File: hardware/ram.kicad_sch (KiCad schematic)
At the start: 1 part, among them U901 MT53E512M32D1ZW-046 WT:B

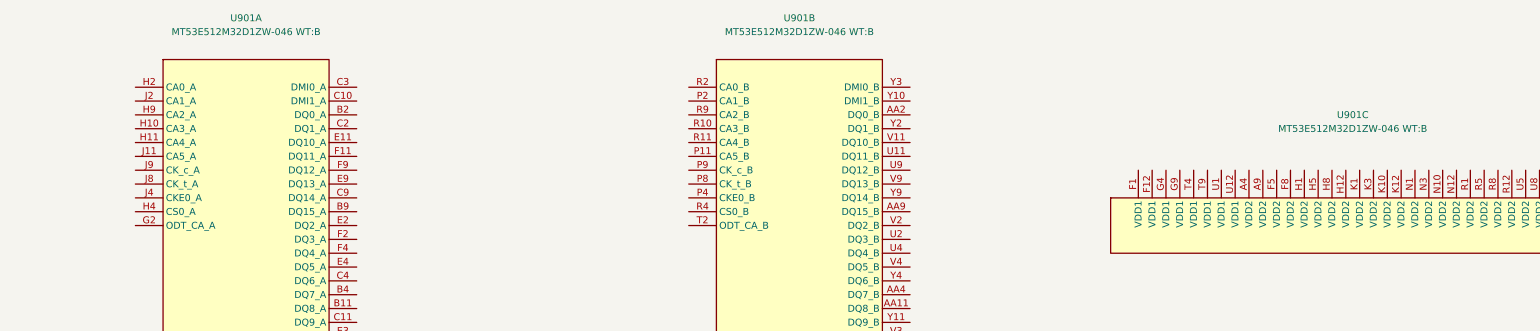
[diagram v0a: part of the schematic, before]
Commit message: Connect RAM VDD1 and LPDDR4X ODT controls
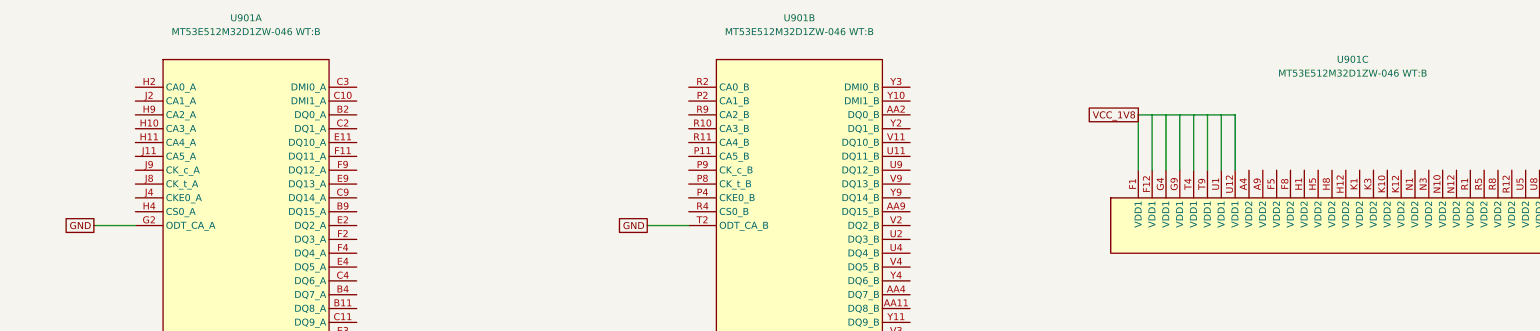
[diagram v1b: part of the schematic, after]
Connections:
- net GND: now also U901.G2 (ODT_CA_A), U901.T2 (ODT_CA_B)
- net VCC_1V8: now reaches U901.F1 (VDD1)
- net VCC_1V8: now also U901.U12 (VDD1)

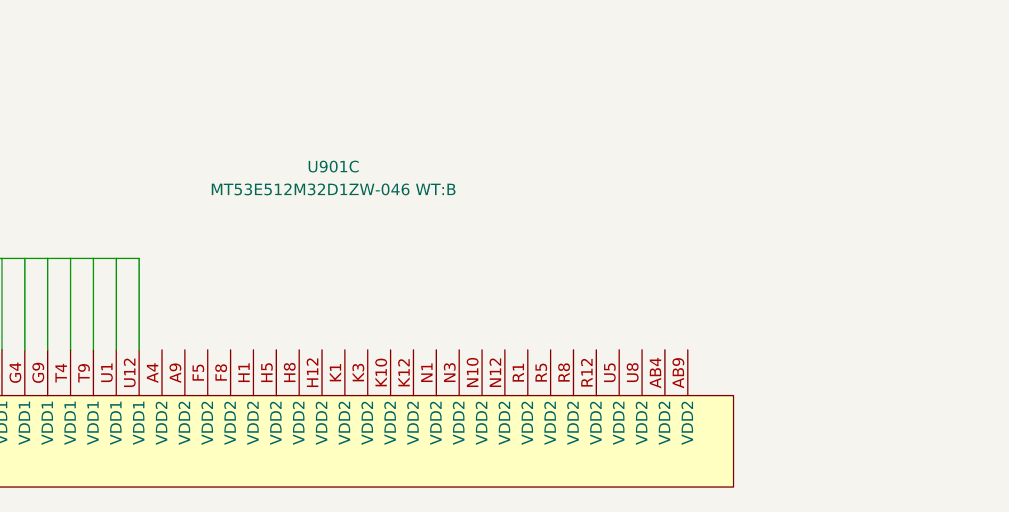
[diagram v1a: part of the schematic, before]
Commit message: Capture DDR BUCK3 supply and RAM VDD2 connections
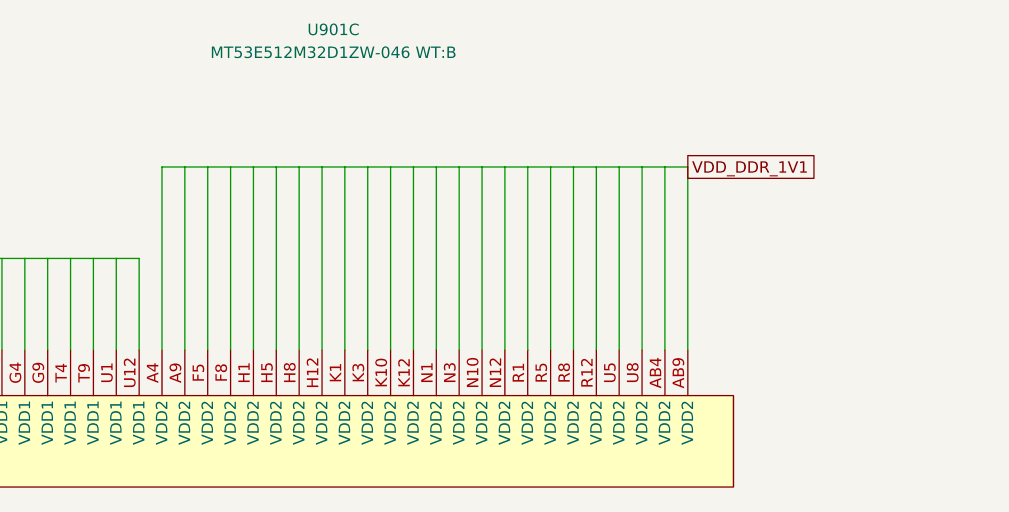
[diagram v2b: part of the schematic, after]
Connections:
- net VDD_DDR_1V1: now reaches U901.A4 (VDD2)
- net VDD_DDR_1V1: now also U901.AB9 (VDD2)

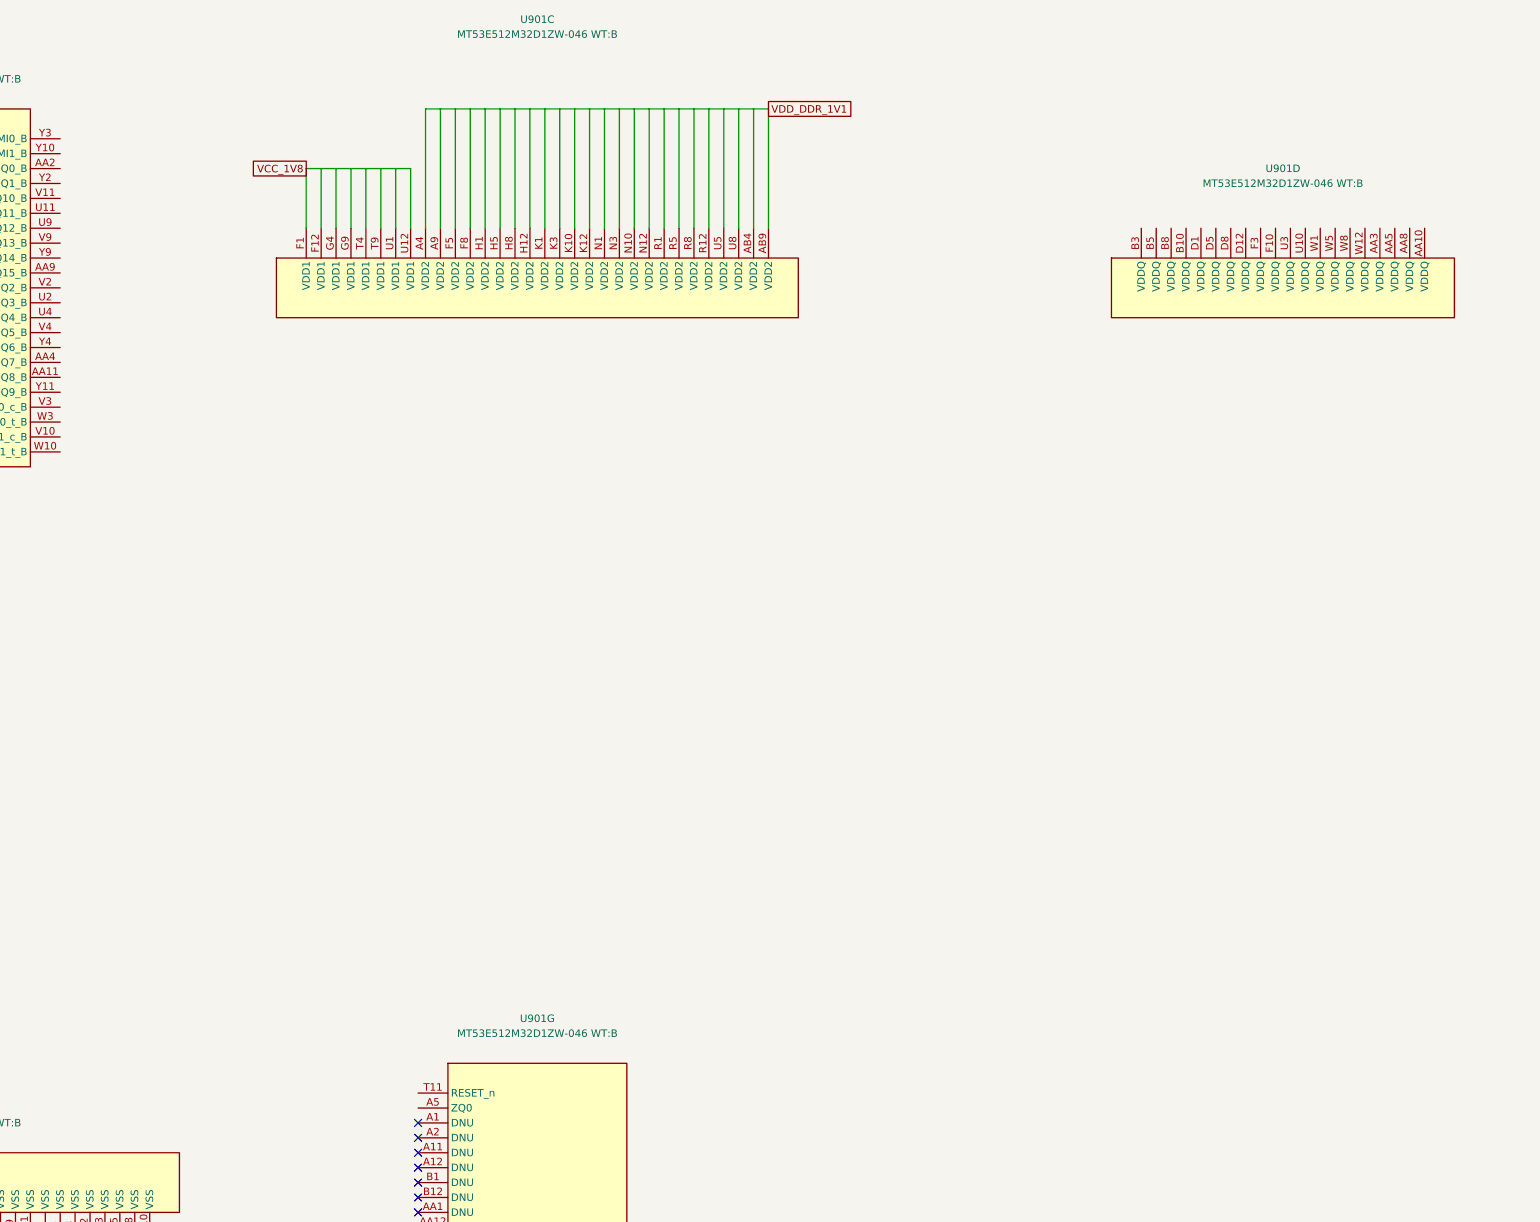
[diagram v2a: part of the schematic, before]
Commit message: Capture RAM ZQ calibration and separate VDDQ domain
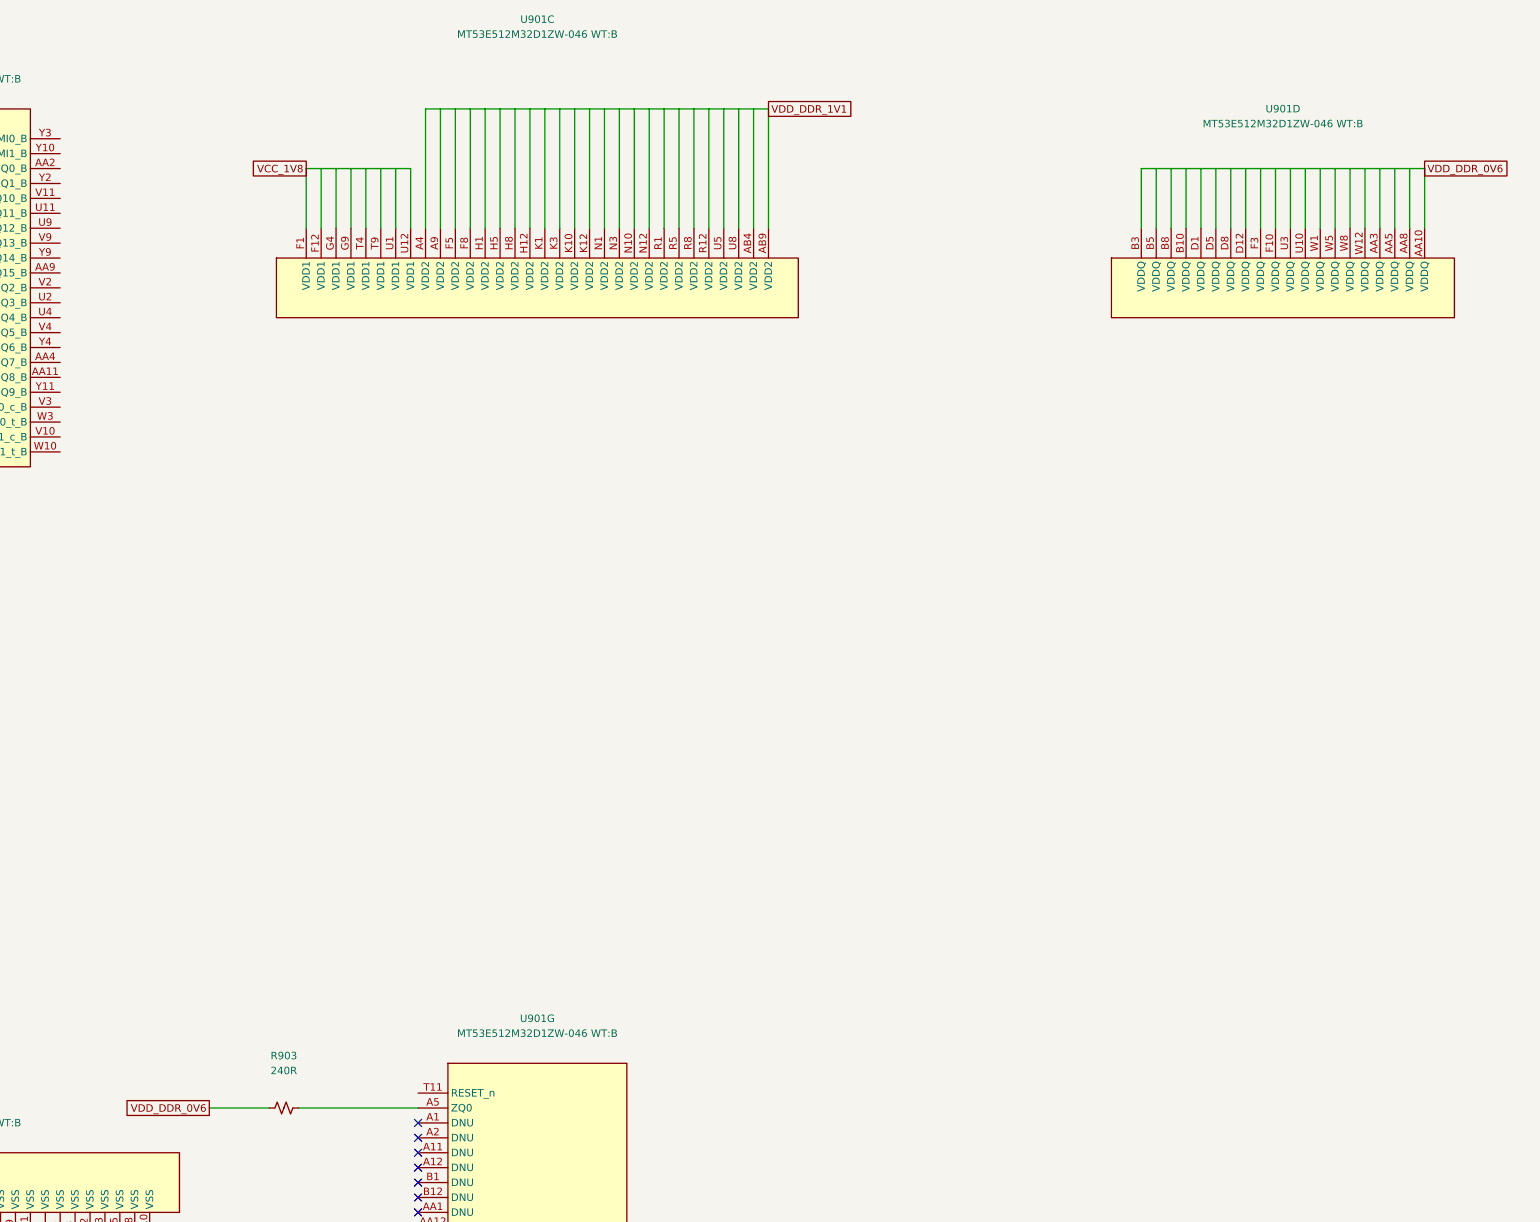
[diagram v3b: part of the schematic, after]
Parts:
- added R903: 240R, Resistor_SMD:R_0603_1608Metric, symbol Device:R_Small_US
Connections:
- net at U901.A5 (ZQ0): now also R903.2
- net VDD_DDR_0V6: now reaches U901.AA10 (VDDQ)
- net VDD_DDR_0V6: now also U901.B3 (VDDQ), R903.1
